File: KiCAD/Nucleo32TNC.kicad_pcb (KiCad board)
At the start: 2 copper layers, 59 x 99 mm, 55 parts, among them J1 AudioJack4, Q1 2N7000, Q2 2N7000, SW1 SW_Push, U1 MCP6004, U2 24LC32

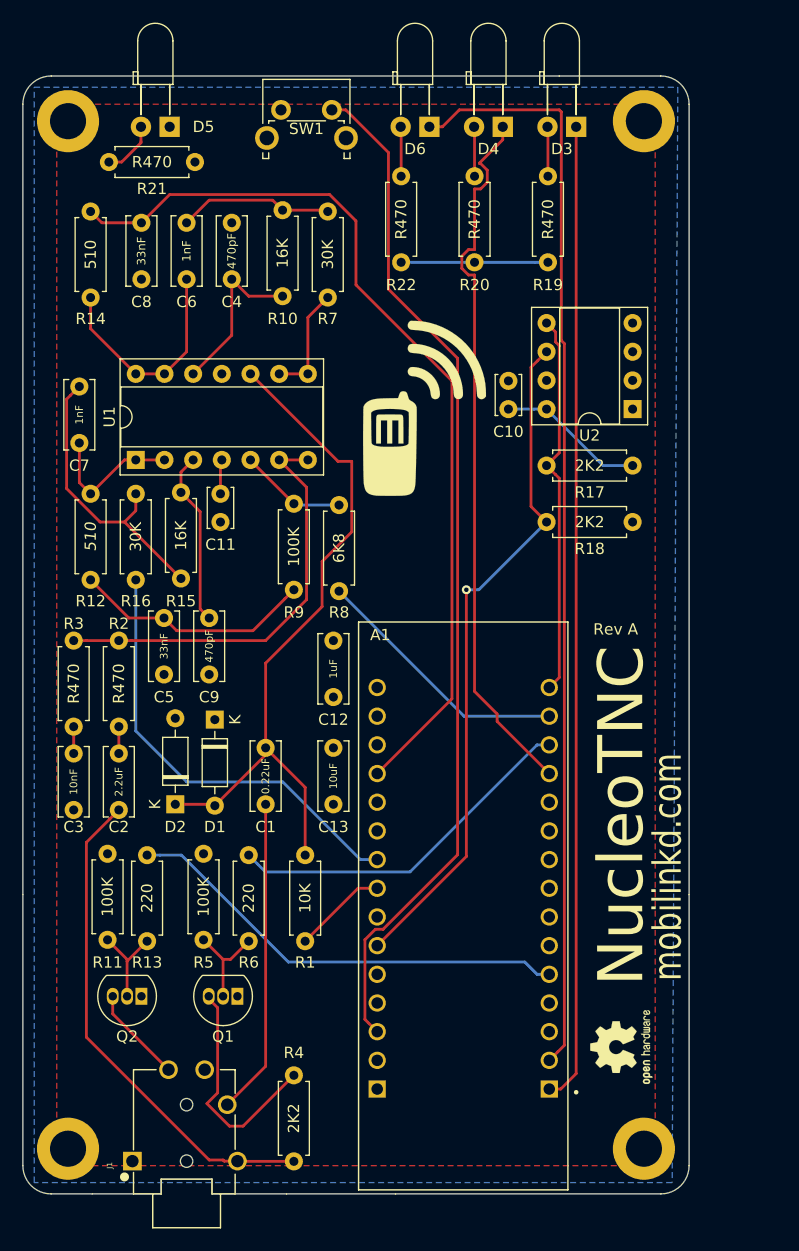
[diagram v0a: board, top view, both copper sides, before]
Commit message: Rev B of 67mm board.  Fix logo, move blue LED a bit, update C1 value, and expand Nucleo pin offsets for press-fit.  Fix hole locations and significant alignment issues in front and rear panels.  Change to panel radius from 4mm to 5mm and height from 25.5mm to 25mm. Simplify and widen spacer.
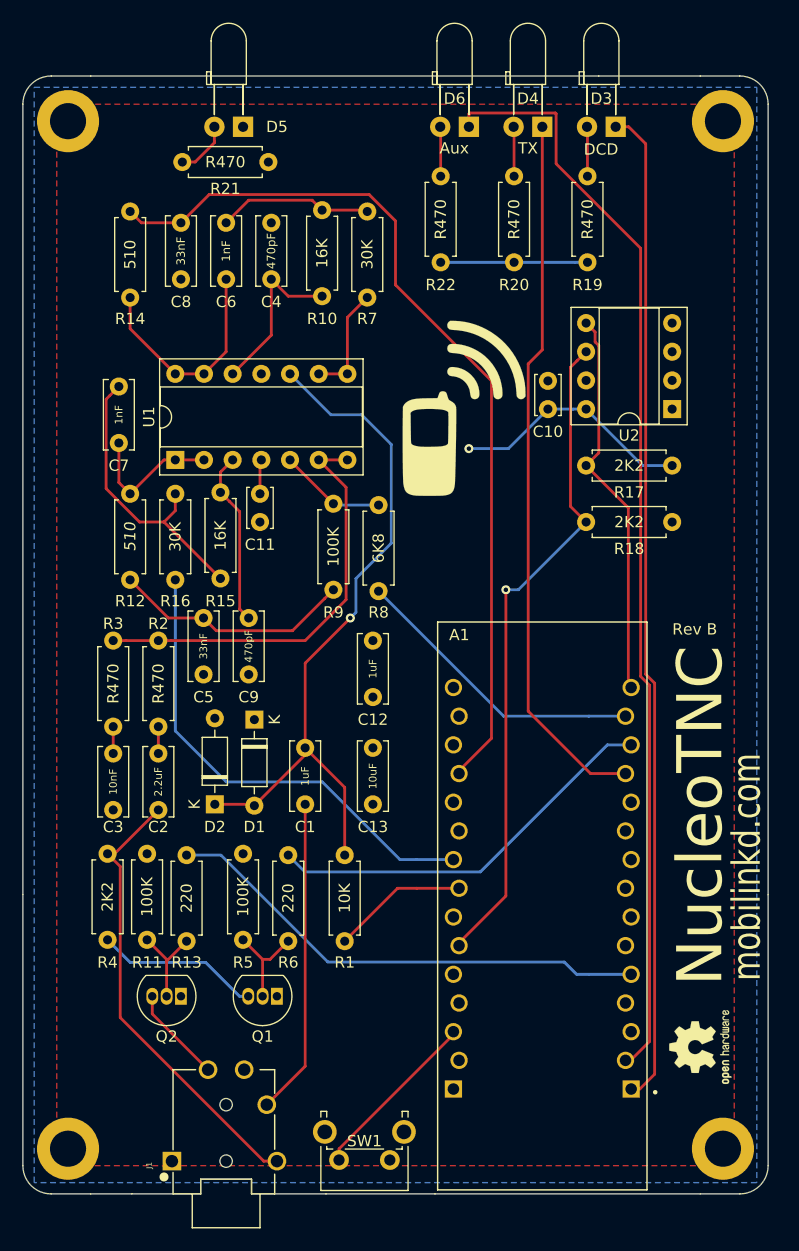
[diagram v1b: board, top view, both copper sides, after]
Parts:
- removed the REF** at (152.5, 81.2)
- C1: value 0.22uF -> 1uF
- D3: value GRN LED -> DCD
- D4: value RED LED -> TX
- D6: value YEL LED -> Aux
- moved SW1 93.5 mm to (152.5, 146.0), turned to 180 degrees
- moved R4 20.4 mm to (127.5, 126.5), turned to 90 degrees
- moved A1 7.00 mm to (166.0, 123.5)
- moved H3 7.00 mm to (182.0, 54.0)
- moved H4 7.00 mm to (182.0, 145.0)
- moved REF** 7.00 mm to (180.0, 136.0)
- moved D5 6.50 mm to (139.5, 54.5)
- moved R21 6.50 mm to (141.7, 57.6)
- moved C1 3.50 mm to (145.0, 109.5)
- moved C10 3.50 mm to (166.5, 79.5)
- moved C11 3.50 mm to (141.0, 87.0)
- moved C12 3.50 mm to (151.0, 105.0)
- moved C13 3.50 mm to (151.0, 109.5)
- moved C2 3.50 mm to (132.0, 115.0)
- moved C3 3.50 mm to (128.0, 115.0)
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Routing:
- net Net-(A1-Pad4.3): track 91.2 -> 15.7 mm
- net +3V3: track 29.1 -> 37.6 mm, vias 0 -> 1
- net Net-(Q1-Pad3): track 20.6 -> 14.5 mm
- net /AUDIO_OUT: track 44.2 -> 40.3 mm
- net /PTT_SIMPLEX: track 40.0 -> 43.5 mm
- net /DC_OFFSET: track 8.32 -> 11.8 mm
- net /DAC_AUDIO: track 39.5 -> 43.0 mm
- net /AUDIO_ATTEN: track 23.2 -> 26.7 mm
- net /PTT_MULTIPLEX: track 31.9 -> 35.4 mm
- net /LED_DCD: track 86.8 -> 88.9 mm
- net /ADC_AUDIO: track 81.1 -> 79.7 mm
- net /I2C_SCL: track 60.6 -> 59.1 mm
- net Net-(C1-Pad1): track 62.2 -> 63.1 mm, vias 0 -> 1
- net /I2C_SDA: track 34.0 -> 34.8 mm
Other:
- board size 59 x 99 mm -> 66 x 99 mm
- board text added: "Rev B"
- board text removed: "Rev A"

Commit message: Add fabrication notes to indicate where to place production codes.
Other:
- board text added: "Please place Production Code here on front silkscreen."
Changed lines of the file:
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@@
   (general
     (thickness 1.6)
-    (drawings 40)
+    (drawings 43)
     (tracks 190)
     (zones 0)
@@
     (visible_elements FFFDFF7F)
     (pcbplotparams
-      (layerselection 0x010f0_ffffffff)
+      (layerselection 0x210f0_ffffffff)
       (usegerberextensions false)
       (usegerberattributes false)
@@
       (drillshape 0)
       (scaleselection 1)
-      (outputdirectory "Gerbers/"))
+      (outputdirectory "Gerbers"))
   )
   (net 0 "")
@@
       (net 6 GND))
   )
+  (gr_text "Please place Production Code here on front silkscreen." (at 198.5 157.5) (layer F.Fab)
+    (effects (font (size 1 1) (thickness 0.15)))
+  )
+  (gr_line (start 168.25 148) (end 191.75 156.5) (layer F.Fab) (width 0.15))
+  (gr_circle (center 166 147.25) (end 167.75 148.5) (layer F.Fab) (width 0.15))
   (dimension 58 (width 0.15) (layer Dwgs.User)
     (gr_text "58.000 mm" (at 153 164.8) (layer Dwgs.User)

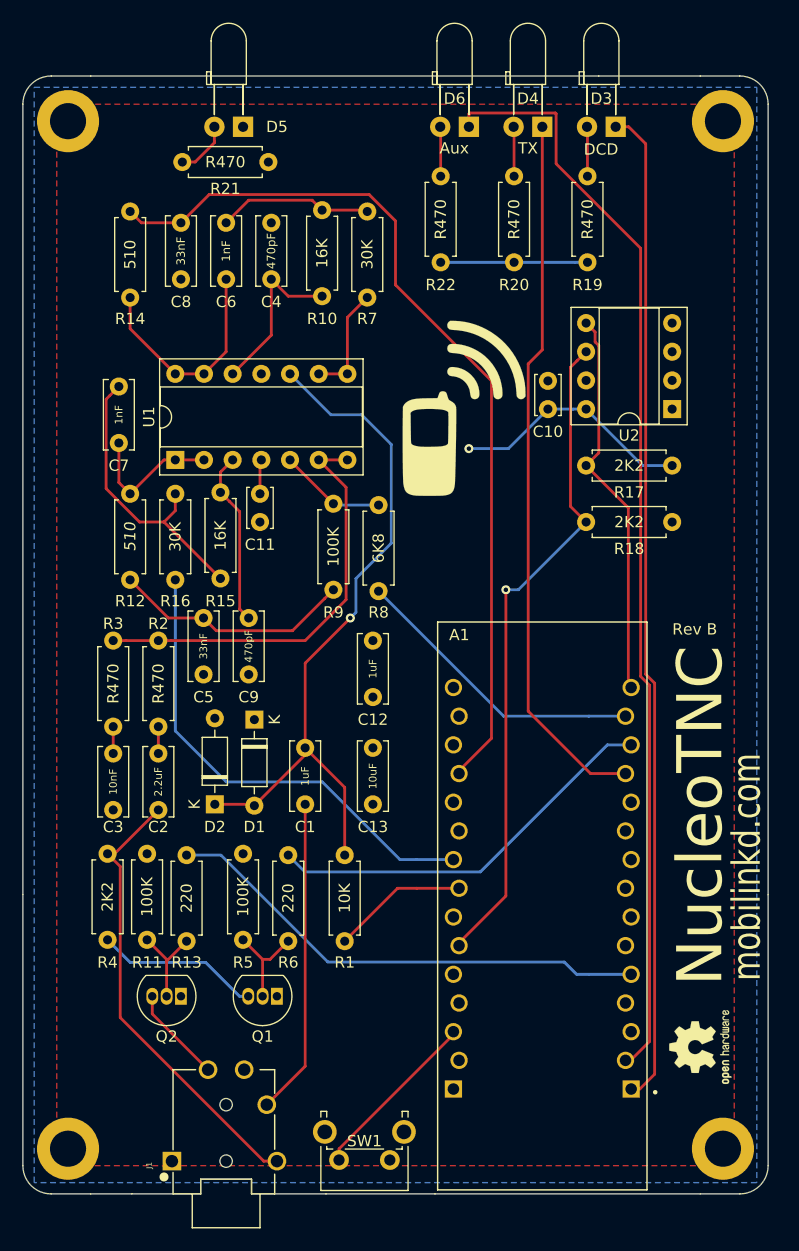
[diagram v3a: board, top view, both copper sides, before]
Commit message: Update PCB to Rev C. Larger footprints for C1, C2, C10, C11, C12, C13, Q1, & Q2. Add new diode D7.
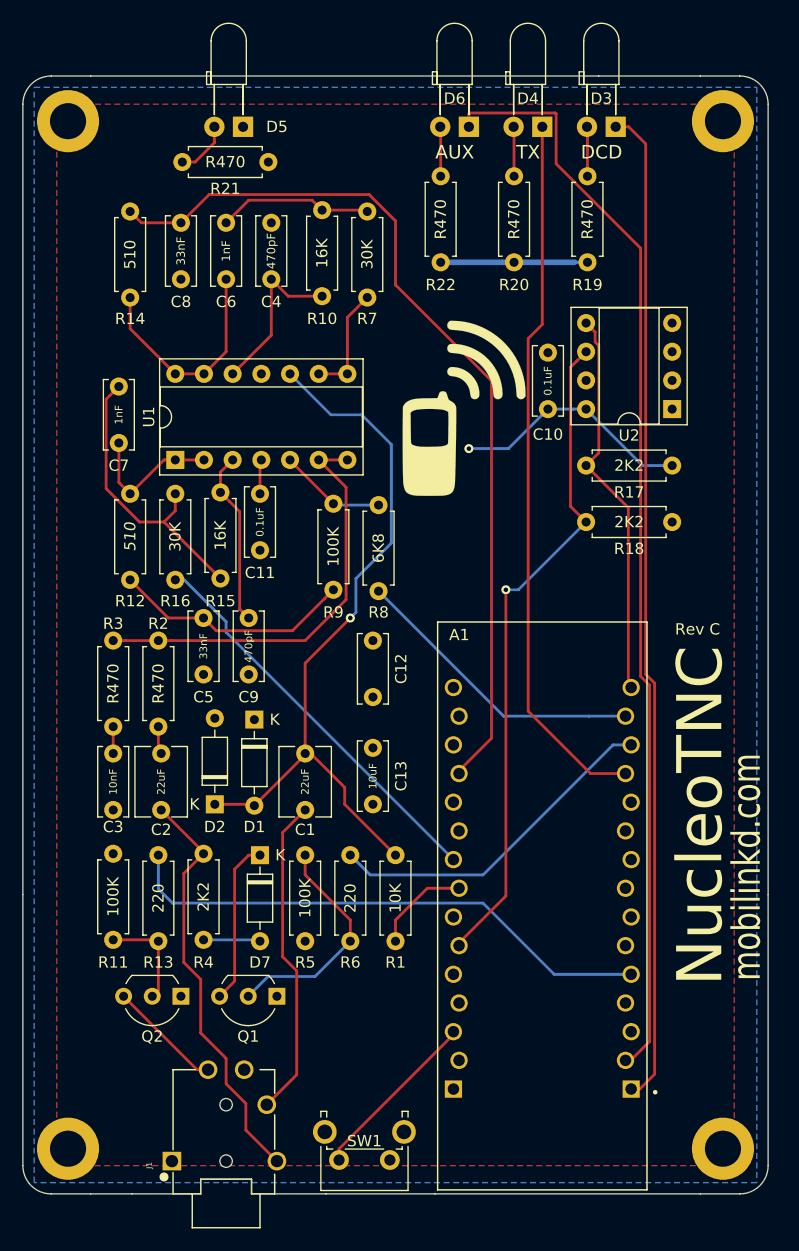
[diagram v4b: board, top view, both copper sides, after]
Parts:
- removed REF**: OSHW-Logo2_7.3x6mm_SilkScreen, Symbol:OSHW-Logo2_7.3x6mm_SilkScreen
- added D7: BAT85, Diode_THT:D_DO-35_SOD27_P7.62mm_Horizontal, F.Cu at (141.0, 119.0)
- C1: value 1uF -> 22uF; footprint Capacitor_THT:C_Disc_D6.0mm_W2.5mm_P5.00mm -> Capacitor_THT:C_Disc_D6.0mm_W4.4mm_P5.00mm
- C10, C11: footprint Capacitor_THT:C_Disc_D3.4mm_W2.1mm_P2.50mm -> Capacitor_THT:C_Disc_D6.0mm_W2.5mm_P5.00mm
- C2: value 2.2uF -> 22uF; footprint Capacitor_THT:C_Disc_D6.0mm_W2.5mm_P5.00mm -> Capacitor_THT:C_Disc_D6.0mm_W4.4mm_P5.00mm
- D3: value DCD -> GRN LED
- D4: value TX -> RED LED
- D6: value Aux -> YEL LED
- H1, H2, H3, H4: value MountingHole -> MountingHole_Pad
- Q1, Q2: footprint Package_TO_SOT_THT:TO-92_Inline -> Package_TO_SOT_THT:TO-92_Inline_Wide
- moved R5 9.30 mm to (145.0, 119.0), turned to 270 degrees
- moved R4 8.50 mm to (136.0, 126.5)
- moved R6 5.50 mm to (149.0, 119.0)
- moved R1 4.50 mm to (153.0, 119.0)
- moved R11 3.00 mm to (128.0, 126.5)
- moved R13 2.50 mm to (132.0, 119.0)
- moved C1 0.50 mm to (145.0, 110.0)
- moved C2 0.25 mm to (132.2, 115.0)
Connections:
- Q1 pad 3: Net-(Q1-Pad3) -> Net-(D7-Pad1)
- R4 pad 1: Net-(Q1-Pad3) -> Net-(D7-Pad2)
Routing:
- net Net-(D7-Pad1): track 0.00 -> 14.6 mm
- net Net-(Q1-Pad3): track 14.5 -> 0.00 mm
- net Net-(Q1-Pad2): track 8.82 -> 20.3 mm
- net /DAC_AUDIO: track 43.0 -> 35.4 mm
- net Net-(D7-Pad2): track 0.00 -> 5.05 mm
- net /PTT_MULTIPLEX: track 35.4 -> 30.4 mm
- net /PTT_SIMPLEX: track 43.5 -> 48.0 mm
- net /AUDIO_OUT: track 40.3 -> 36.8 mm
- net /DC_OFFSET: track 11.8 -> 8.67 mm
- net Net-(C1-Pad1): track 63.1 -> 64.9 mm
- net /PTT: track 8.55 -> 10.2 mm
- net Net-(Q2-Pad2): track 8.22 -> 9.15 mm
- net /AUDIO_IN: track 28.0 -> 28.5 mm
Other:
- net class Power added: clearance 0.2, trace_width 0.5, via_dia 0.8, via_drill 0.4
- board text added: "AUX"
- board text added: "DCD"
- board text added: "Rev C"
- board text added: "TX"
- board text removed: "Rev B"

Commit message: Fix a small silkscreen error.  Move part designators for op amp, EEPROM and Nucleo board to silkscreen.
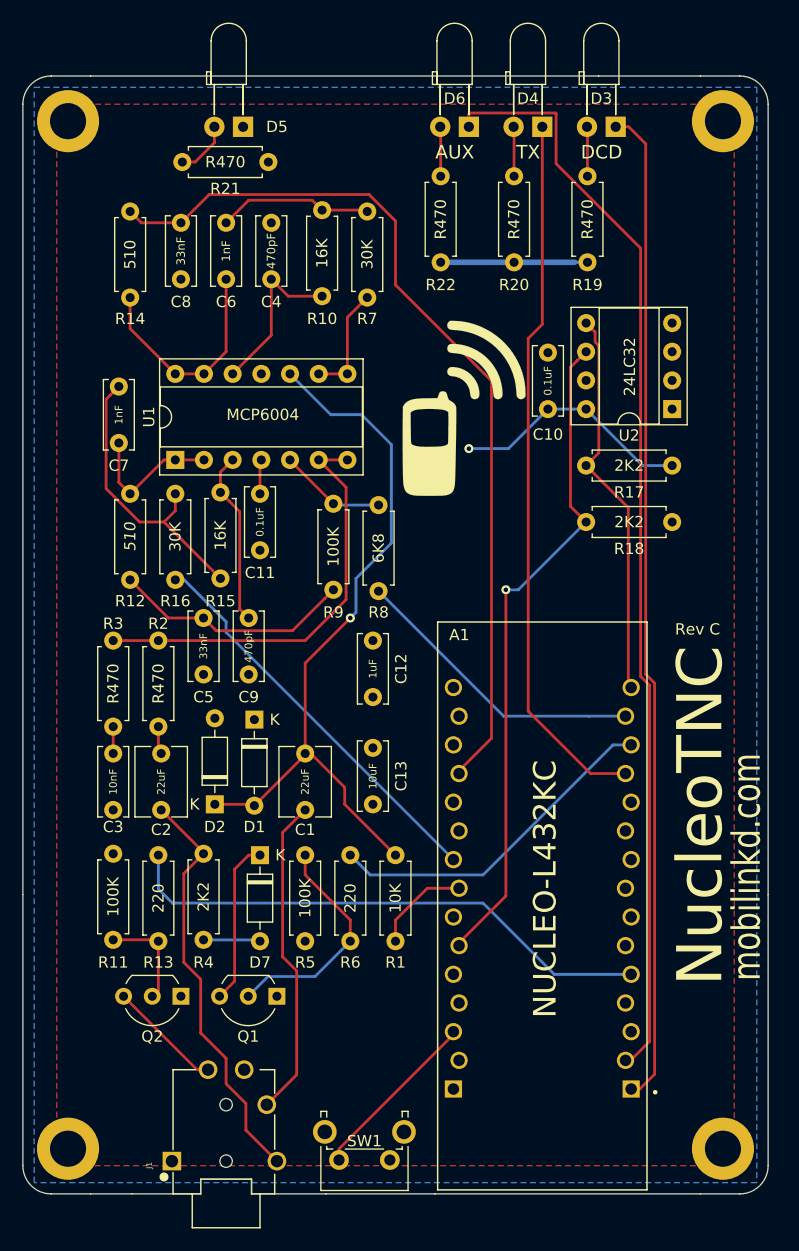
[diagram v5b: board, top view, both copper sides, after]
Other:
- rule pad_to_mask_clearance: 0.051 -> 0
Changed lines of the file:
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@@
   )
   (layers
-    (0 F.Cu signal)
+    (0 F.Cu signal hide)
     (31 B.Cu signal)
     (32 B.Adhes user hide)
@@
     (pad_size 1.53 1.53)
     (pad_drill 1.02)
-    (pad_to_mask_clearance 0.051)
-    (solder_mask_min_width 0.25)
+    (pad_to_mask_clearance 0)
     (aux_axis_origin 0 0)
     (grid_origin 120 50)
@@
       (effects (font (size 1 1) (thickness 0.15)))
     )
-    (fp_text value 1uF (at 2.5 0 90) (layer F.Fab)
+    (fp_text value 1uF (at 2.5 0 90) (layer F.SilkS)
       (effects (font (size 0.68 0.68) (thickness 0.11)))
     )
@@
       (effects (font (size 1 1) (thickness 0.015)))
     )
-    (fp_text value NUCLEO-L432KC (at 3.81 26.035 180) (layer F.Fab)
-      (effects (font (size 1 1) (thickness 0.015)))
+    (fp_text value NUCLEO-L432KC (at -0.25 1.5 270) (layer F.SilkS)
+      (effects (font (size 2 2) (thickness 0.3)))
     )
     (fp_line (start -9.27 -25.145) (end 9.27 -25.145) (layer F.Fab) (width 0.127))
@@
       (effects (font (size 1 1) (thickness 0.15)))
     )
-    (fp_text value 24LC32 (at 3.81 9.95) (layer F.Fab)
+    (fp_text value 24LC32 (at 3.75 3.75 90) (layer F.SilkS)
       (effects (font (size 1 1) (thickness 0.15)))
     )
@@
     (fp_line (start 9.15 9.2) (end 9.15 -1.6) (layer F.CrtYd) (width 0.05))
     (fp_line (start 9.15 -1.6) (end -1.55 -1.6) (layer F.CrtYd) (width 0.05))
-    (fp_text user %R (at 3.81 3.81) (layer F.Fab)
+    (fp_text user %R (at 3.81 -2.25) (layer F.Fab)
       (effects (font (size 1 1) (thickness 0.15)))
     )
@@
       (effects (font (size 1 1) (thickness 0.15)))
     )
-    (fp_text value MCP6004 (at 3.81 17.57 90) (layer F.Fab)
+    (fp_text value MCP6004 (at 4 7.75 180) (layer F.SilkS)
       (effects (font (size 1 1) (thickness 0.15)))
     )
@@
     (fp_line (start 9.15 16.85) (end 9.15 -1.6) (layer F.CrtYd) (width 0.05))
     (fp_line (start 9.15 -1.6) (end -1.55 -1.6) (layer F.CrtYd) (width 0.05))
-    (fp_text user %R (at 3.81 7.62 90) (layer F.Fab)
-      (effects (font (size 1 1) (thickness 0.15)))
-    )
+    (fp_text user %R (at 3.81 -2.25 90) (layer F.Fab)
+      (effects (font (size 1 1) (thickness 0.15)))
+    )
